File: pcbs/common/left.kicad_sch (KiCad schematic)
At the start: 88 parts

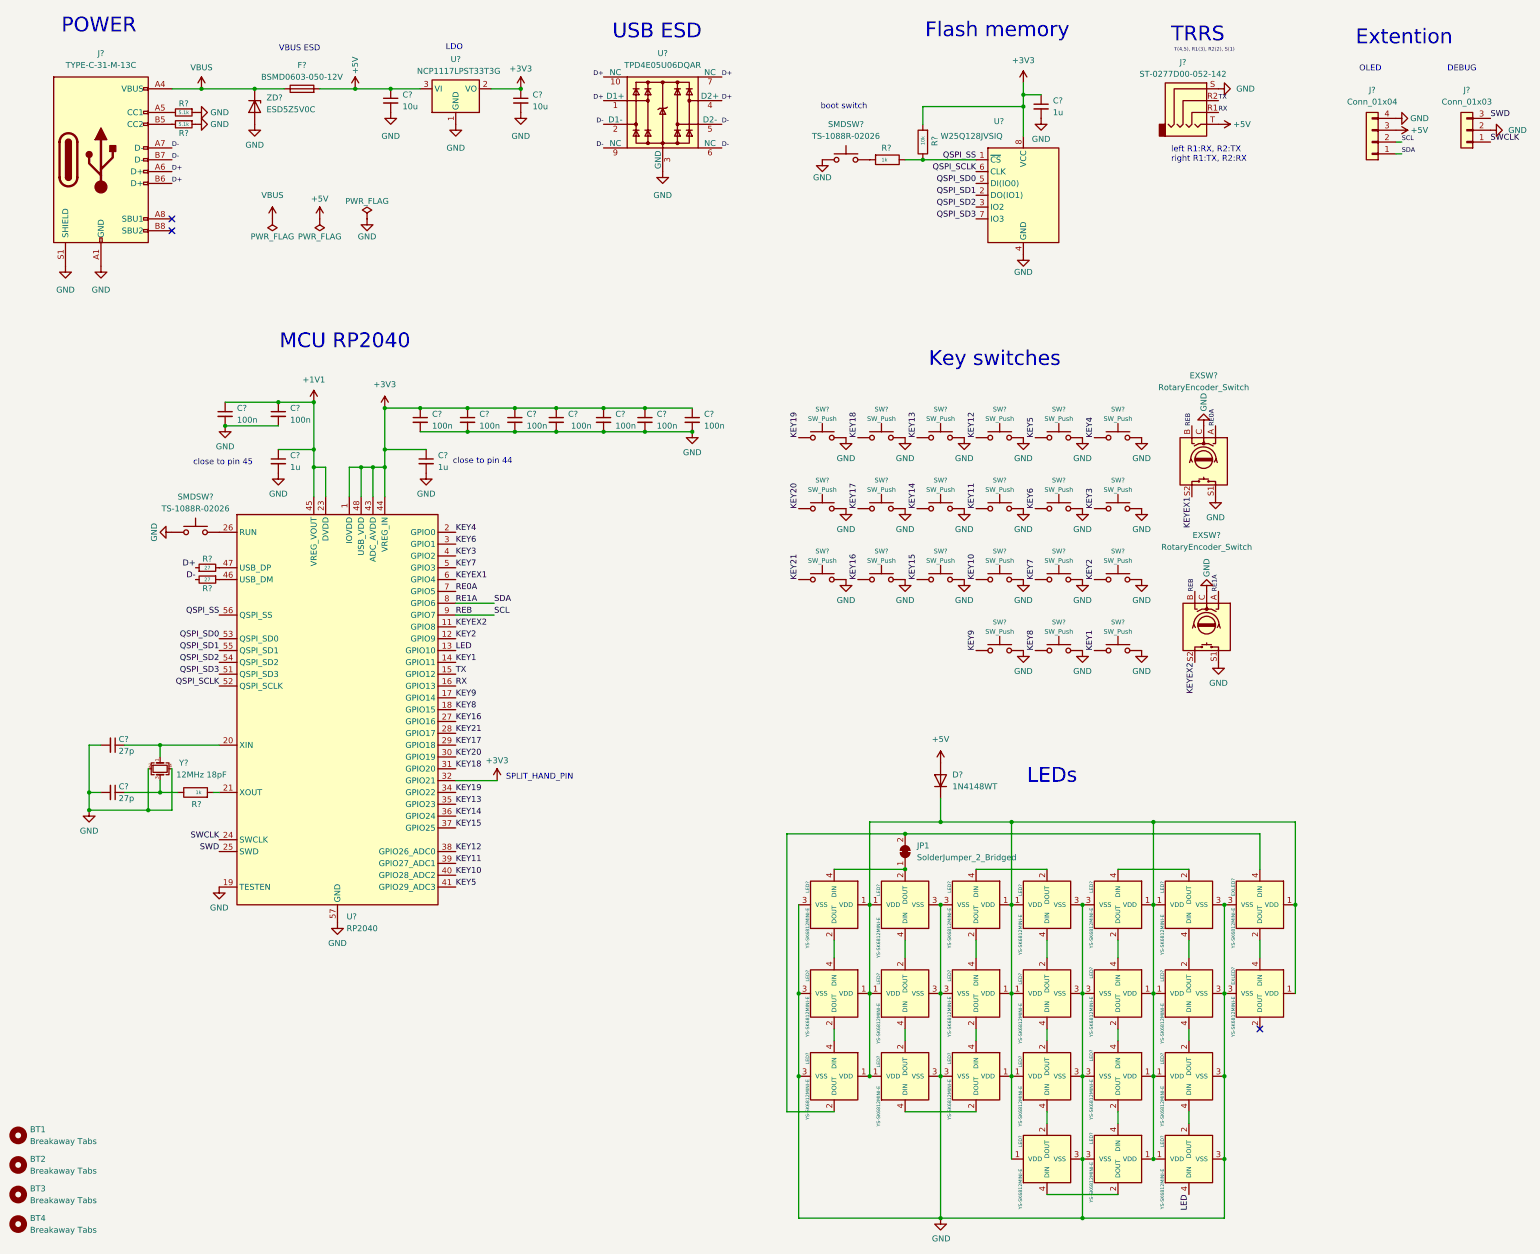
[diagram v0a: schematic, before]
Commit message: replaced trrs with USB-C
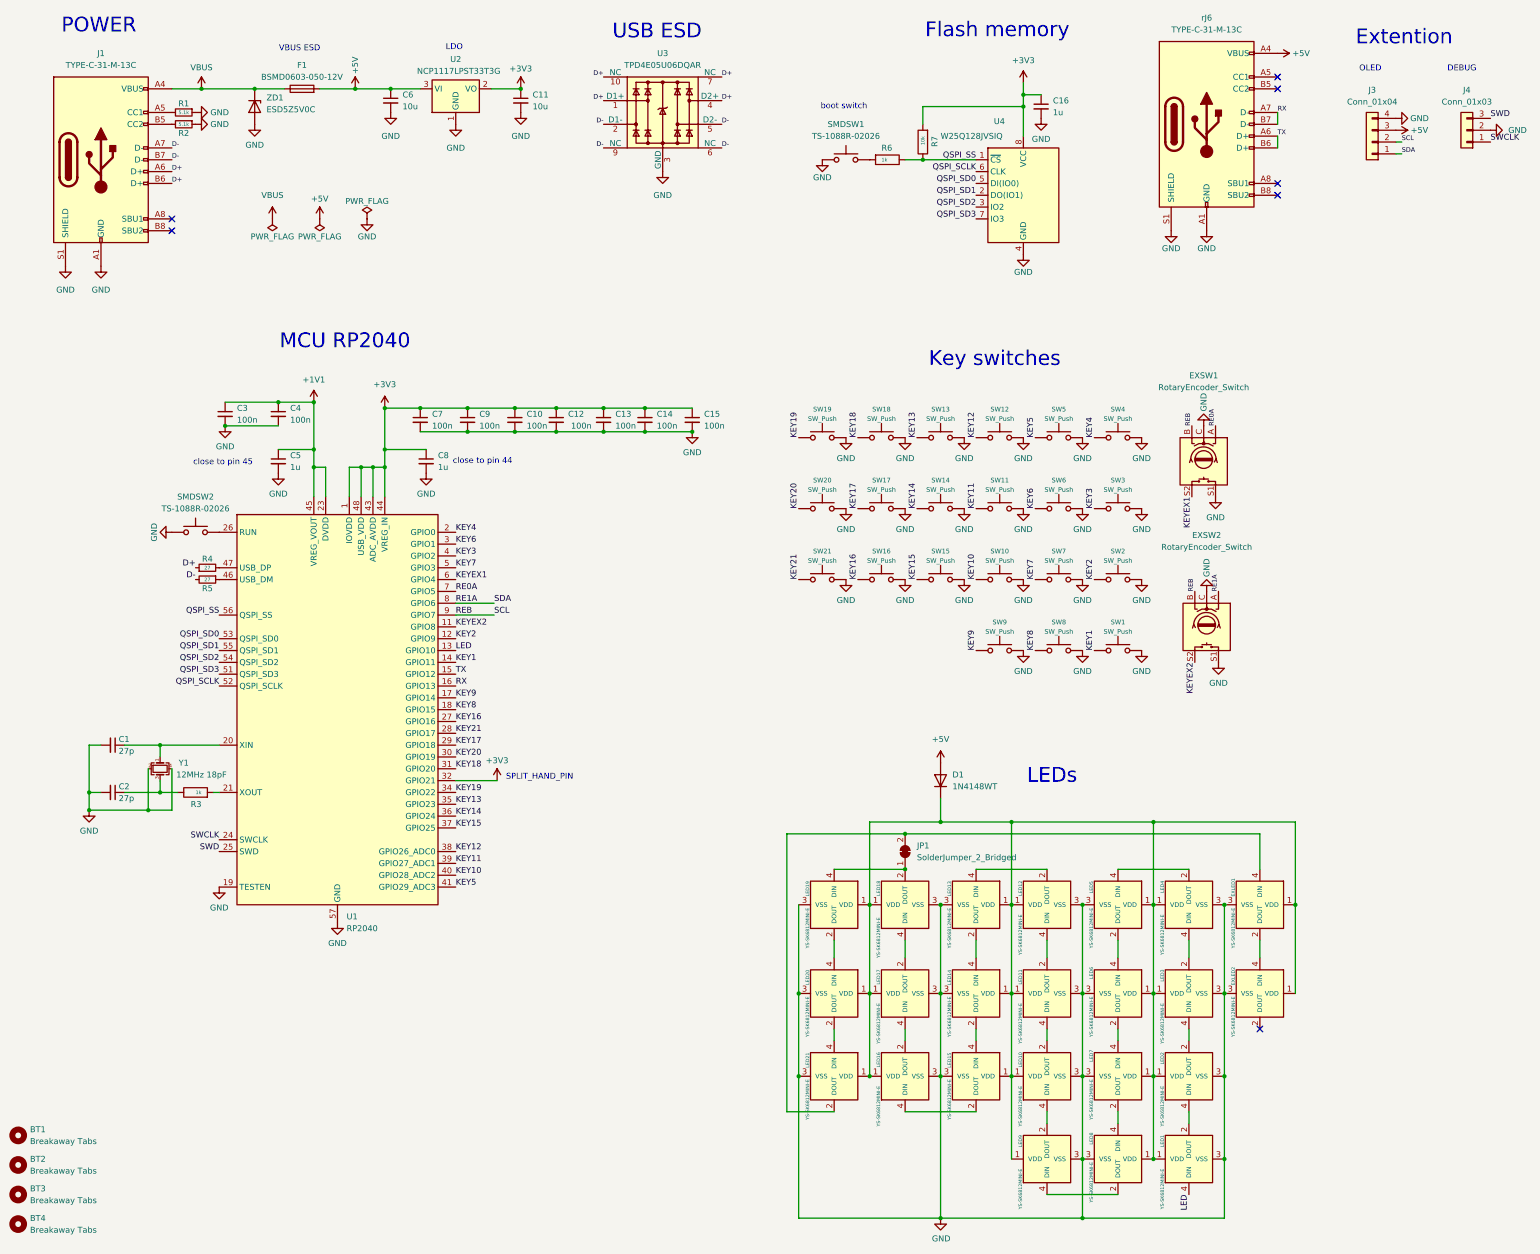
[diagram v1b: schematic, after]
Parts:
- removed J?: ST-0277D00-052-142, kbd_local:ST-0277D00-052-142, symbol Connector_Audio:AudioJack4
- added rJ6: TYPE-C-31-M-13C, kbd_local:TYPE-C-31-M-13C, symbol Connector:USB_C_Receptacle_USB2.0
- gave numbers to parts that had none: 82
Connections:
- net +5V: now also rJ6.A4 (VBUS), rJ6.A9 (VBUS), rJ6.B4 (VBUS), rJ6.B9 (VBUS)
- net GND: now also rJ6.A1 (GND), rJ6.A12 (GND), rJ6.B1 (GND), rJ6.B12 (GND), rJ6.S1 (SHIELD)
- net RX: now also rJ6.A7 (D-), rJ6.B7 (D-)
- net TX: now also rJ6.A6 (D+), rJ6.B6 (D+)
- no-connect marks 3 -> 7
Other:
- note removed: "T(4,5), R1(3), R2(2), S(1)"
- note removed: "TRRS"
- note removed: "left R1:RX, R2:TX right R1:TX, R2:RX"
